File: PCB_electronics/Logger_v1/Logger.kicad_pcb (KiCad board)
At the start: 2 copper layers, 1 part

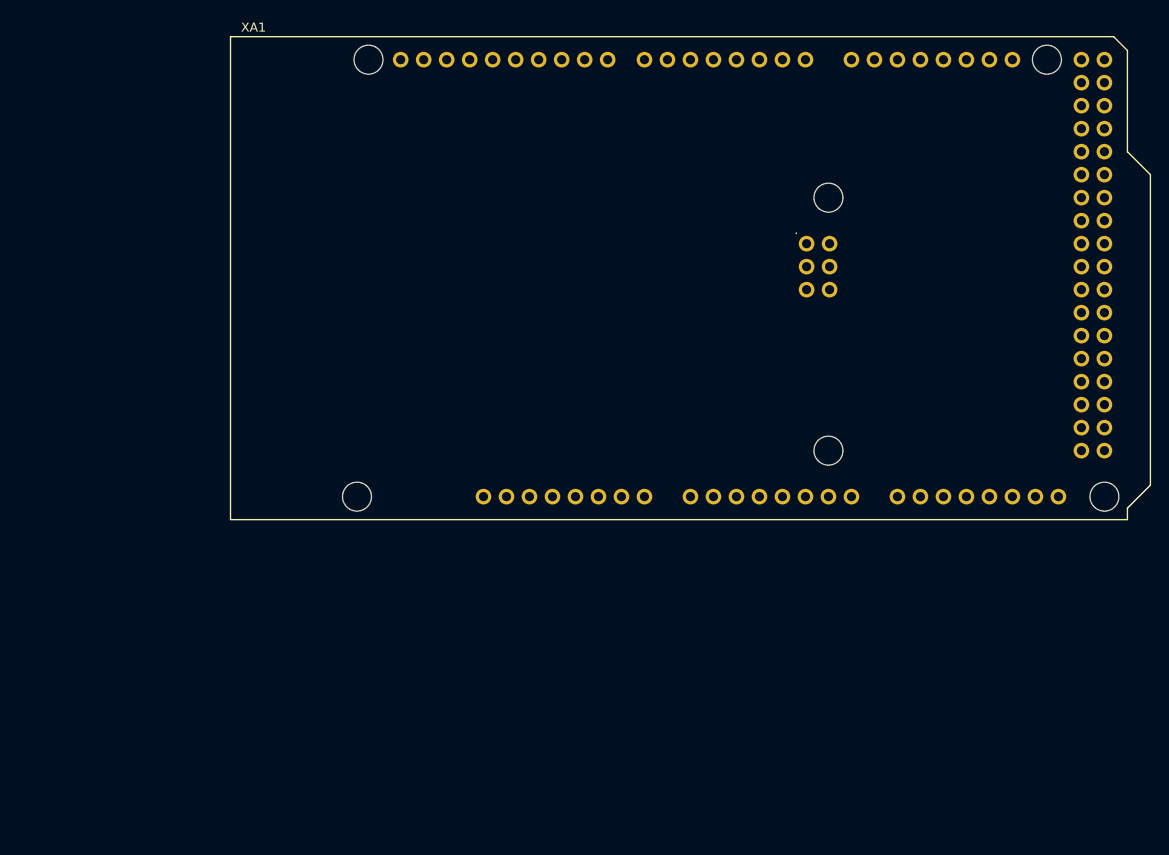
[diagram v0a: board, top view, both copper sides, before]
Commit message: placed components 1
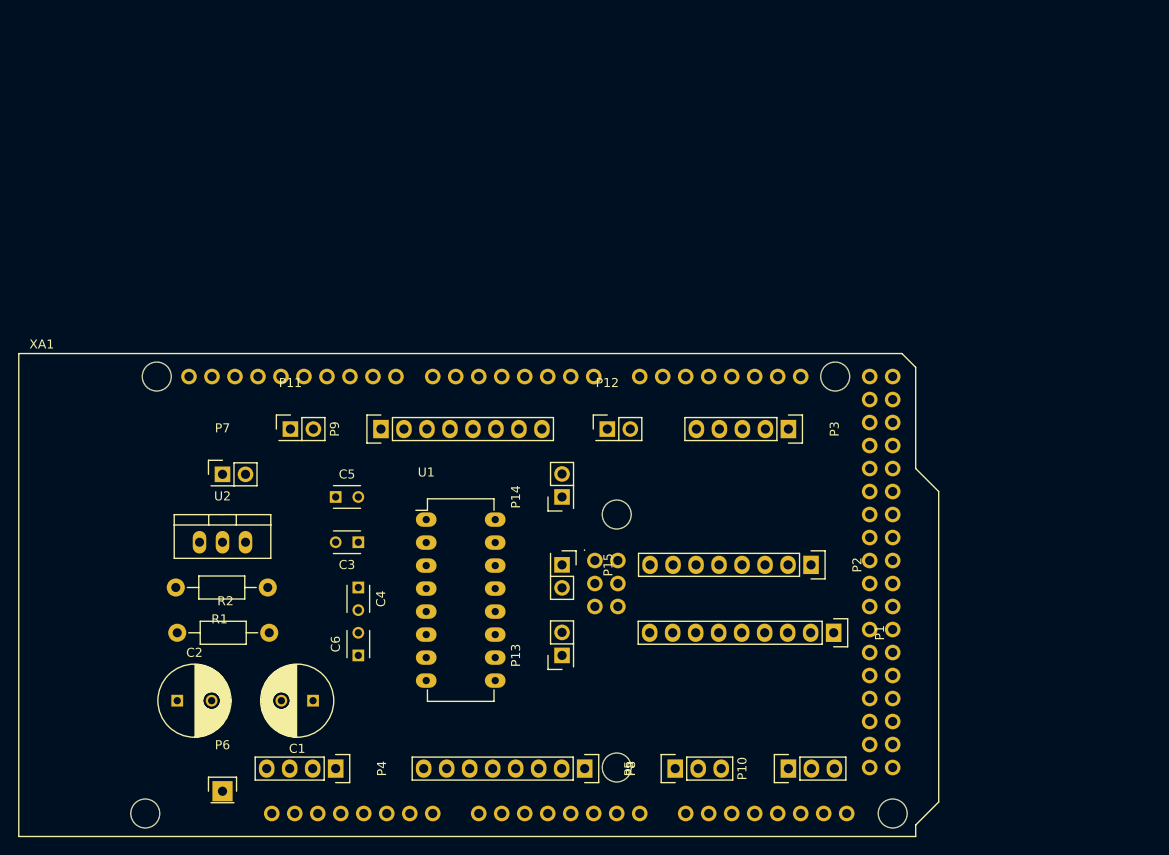
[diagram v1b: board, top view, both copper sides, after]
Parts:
- added C1: 1uF, Capacitors_ThroughHole:C_Radial_D8_L11.5_P3.5, F.Cu at (145.0, 125.0)
- added C2: 1000uF, Capacitors_ThroughHole:C_Radial_D8_L13_P3.8, F.Cu at (130.0, 125.0)
- added C3: 1.0uF, Capacitors_ThroughHole:C_Disc_D3_P2.5, F.Cu at (150.0, 107.5)
- added C4: 1.0uF, Capacitors_ThroughHole:C_Disc_D3_P2.5, F.Cu at (150.0, 112.5)
- added C5: 1.0uF, Capacitors_ThroughHole:C_Disc_D3_P2.5, F.Cu at (147.5, 102.5)
- added C6: 1.0uF, Capacitors_ThroughHole:C_Disc_D3_P2.5, F.Cu at (150.0, 120.0)
- added P1: GPS_breakout_connector, Pin_Headers:Pin_Header_Straight_1x09, F.Cu at (202.5, 117.5)
- added P10: CONN_01X03, Pin_Headers:Pin_Header_Straight_1x03, F.Cu at (197.5, 132.5)
- added P11: CONN_01X02, Pin_Headers:Pin_Header_Straight_2x01, F.Cu at (142.5, 95.0)
- added P12: CONN_01X02, Pin_Headers:Pin_Header_Straight_2x01, F.Cu at (177.5, 95.0)
- added P13: CONN_01X02, Pin_Headers:Pin_Header_Straight_2x01, F.Cu at (172.5, 120.0)
- added P14: CONN_01X02, Pin_Headers:Pin_Header_Straight_2x01, F.Cu at (172.5, 102.5)
- added P15: CONN_01X02, Pin_Headers:Pin_Header_Straight_2x01, F.Cu at (172.5, 110.0)
- added P2: SD_breakout_connector, Pin_Headers:Pin_Header_Straight_1x08, F.Cu at (200.0, 110.0)
- added P3: Iridium_connector, Pin_Headers:Pin_Header_Straight_1x05, F.Cu at (197.5, 95.0)
- added P4: VN100_connector, Pin_Headers:Pin_Header_Straight_1x04, F.Cu at (147.5, 132.5)
- added P5: PowerManager_connector, Pin_Headers:Pin_Header_Straight_1x03, F.Cu at (185.0, 132.5)
- added P6: BATT_connector, Pin_Headers:Pin_Header_Straight_1x01, F.Cu at (135.0, 135.0)
- added P7: RPI_connector, Pin_Headers:Pin_Header_Straight_2x01, F.Cu at (135.0, 100.0)
- added P8: CONN_01X08, Pin_Headers:Pin_Header_Straight_1x08, F.Cu at (175.0, 132.5)
- added P9: CONN_01X08, Pin_Headers:Pin_Header_Straight_1x08, F.Cu at (152.5, 95.0)
- added R1: 46k, Resistors_ThroughHole:Resistor_Horizontal_RM10mm, F.Cu at (140.0, 112.5)
- added R2: 32k, Resistors_ThroughHole:Resistor_Horizontal_RM10mm, F.Cu at (130.0, 117.5)
- added U1: MAX232, Housings_DIP:DIP-16_W7.62mm_LongPads, F.Cu at (157.5, 105.0)
- added U2: FQP27P06, TO_SOT_Packages_THT:TO-220_Neutral123_Vertical, F.Cu at (135.0, 107.5)
- moved XA1 42.1 mm to (112.5, 140.0)
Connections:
- XA1 pad 5V1: Net-(XA1-Pad5V1) -> +5V
- XA1 pad 5V3: Net-(XA1-Pad5V3) -> +5V
- XA1 pad 5V4: Net-(XA1-Pad5V4) -> +5V
- XA1 pad A0: Net-(XA1-PadA0) -> /BATT_+
- XA1 pad A1: Net-(XA1-PadA1) -> /ANALOG_8
- XA1 pad A2: Net-(XA1-PadA2) -> /ANALOG_7
- XA1 pad A3: Net-(XA1-PadA3) -> /ANALOG_6
- XA1 pad A4: Net-(XA1-PadA4) -> /ANALOG_5
- XA1 pad A5: Net-(XA1-PadA5) -> /ANALOG_4
- XA1 pad A6: Net-(XA1-PadA6) -> /ANALOG_3
- XA1 pad A7: Net-(XA1-PadA7) -> /ANALOG_2
- XA1 pad A8: Net-(XA1-PadA8) -> /ANALOG_1
- XA1 pad D0: Net-(XA1-PadD0) -> /RX0
- XA1 pad D1: Net-(XA1-PadD1) -> /TX0
- XA1 pad D14: Net-(XA1-PadD14) -> /TX3
- XA1 pad D15: Net-(XA1-PadD15) -> /RX3
- XA1 pad D16: Net-(XA1-PadD16) -> /IRD_TXD
- XA1 pad D17: Net-(XA1-PadD17) -> /IRD_RXC
- XA1 pad D18: Net-(XA1-PadD18) -> /MEGA_TX_1
- XA1 pad D19: Net-(XA1-PadD19) -> /MEGA_RX_1
- XA1 pad D2: Net-(XA1-PadD2) -> /DGTL_8
- XA1 pad D3: Net-(XA1-PadD3) -> /DGTL_7
- XA1 pad D4: Net-(XA1-PadD4) -> /DGTL_6
- XA1 pad D46: Net-(XA1-PadD46) -> /RPI_control
- XA1 pad D48: Net-(XA1-PadD48) -> /MEGA_feedback
- XA1 pad D49: Net-(XA1-PadD49) -> /IRD_ON_OFF
- XA1 pad D5: Net-(XA1-PadD5) -> /DGTL_5
- XA1 pad D50: Net-(XA1-PadD50) -> /MISO
- XA1 pad D51: Net-(XA1-PadD51) -> /MOSI
- XA1 pad D52: Net-(XA1-PadD52) -> /SCK
- XA1 pad D53: Net-(XA1-PadD53) -> /SS
- XA1 pad D6: Net-(XA1-PadD6) -> /DGTL_4
- XA1 pad D7: Net-(XA1-PadD7) -> /DGTL_3
- XA1 pad D8: Net-(XA1-PadD8) -> /DGTL_2
- XA1 pad D9: Net-(XA1-PadD9) -> /DGTL_1
- XA1 pad GND1: Net-(XA1-PadGND1) -> GND
- XA1 pad GND2: Net-(XA1-PadGND2) -> GND
- XA1 pad GND3: Net-(XA1-PadGND3) -> GND
- XA1 pad GND5: Net-(XA1-PadGND5) -> GND
- XA1 pad GND6: Net-(XA1-PadGND6) -> GND
- XA1 pad SCL: Net-(XA1-PadSCL) -> /SCL
- XA1 pad SDA: Net-(XA1-PadSDA) -> /SDA
